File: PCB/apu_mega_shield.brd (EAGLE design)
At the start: 108 x 54.4 mm, 46 parts, among them IC1 74AHC573, IC2 4050D, IC3 DS1307, IC4 LP298XS, Q1 32.768, U1 IS62C1024AL, X1 MICROSDMOLEX

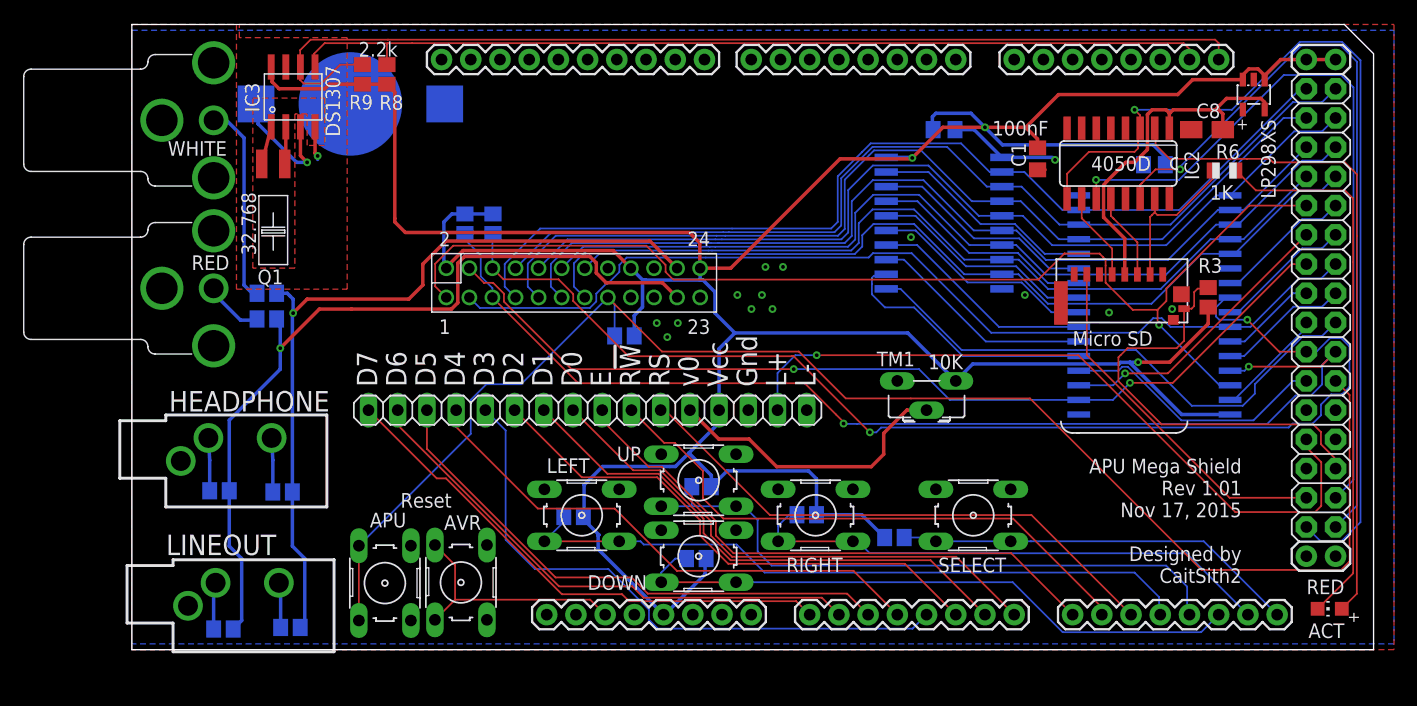
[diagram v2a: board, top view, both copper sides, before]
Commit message: Tweaked reset button layouts.  On the module version of the board, SD card connector and its supporting components moved.
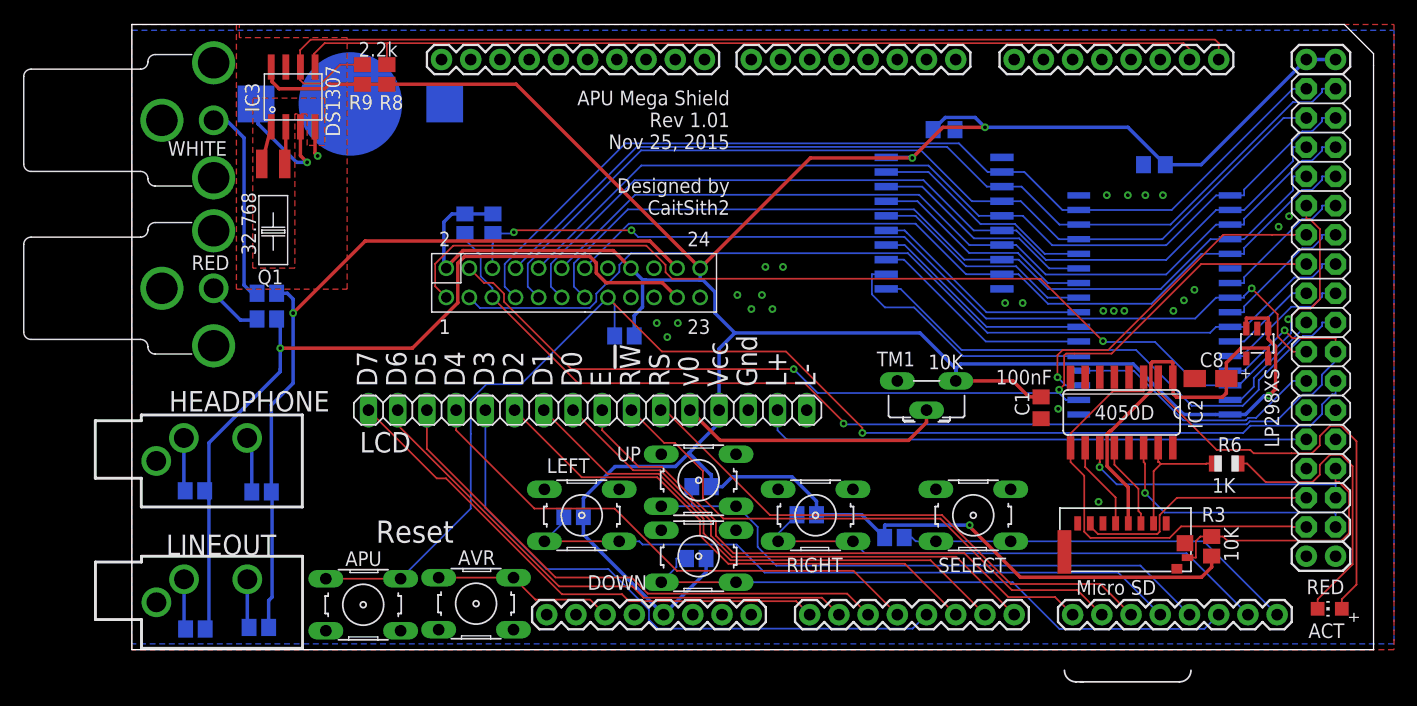
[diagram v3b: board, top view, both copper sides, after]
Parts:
- moved R6 25.5 mm to (95.2, 16.2)
- moved C8 21.6 mm to (93.8, 23.6)
- moved C1 21.6 mm to (79.0, 21.0)
- moved IC2 21.6 mm to (86.1, 20.6)
- moved IC4 21.6 mm to (97.8, 26.6)
- moved R3 21.6 mm to (93.9, 8.99)
- moved X1 21.6 mm to (81.1, 6.81)
- moved U$3 2.76 mm to (6.84, 4.12)
- moved C5 2.74 mm to (11.0, 1.94)
- moved APU 2.66 mm to (20.1, 3.91), turned to 180 degrees
- moved C6 2.44 mm to (5.52, 1.80)
- moved AVR 2.27 mm to (29.9, 4.00), turned to 180 degrees
- moved R5 2.13 mm to (5.49, 13.8)
- moved U$2 2.13 mm to (6.82, 16.4)
- moved R4 1.83 mm to (11.3, 13.7)
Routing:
- net CS: track 67.0 -> 22.5 mm
- net CLK: track 81.7 -> 38.1 mm, vias 1 -> 0
- net DI: track 64.6 -> 24.0 mm
- net !RD: track 105.5 -> 81.6 mm, vias 2 -> 3
- net N$11: track 48.1 -> 26.2 mm
- net BUF_LED: track 58.4 -> 37.8 mm
- net RST: track 133.2 -> 115.2 mm, vias 0 -> 1
- net VCC: track 314.0 -> 331.1 mm, vias 3 -> 4
- net CD: track 37.9 -> 22.3 mm
- net N$14: track 63.3 -> 48.1 mm, vias 1 -> 0
- net GND: track 13.4 -> 2.63 mm, vias 15 -> 26
- net DO: track 31.2 -> 21.5 mm
- net N$1: track 21.5 -> 15.8 mm
- net A13: track 25.2 -> 30.1 mm
- net A11: track 82.8 -> 85.9 mm
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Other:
- board text added: "APU Mega Shield Rev 1.01 Nov 25, 2015 Designed by CaitSith2"
- board text removed: "APU Mega Shield Rev 1.01 Nov 17, 2015 Designed by CaitSith2"

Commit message: Final revisions to the PCB design, hopefully. :)
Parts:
- added C9: 100nF, apu_pcb:C0805
- C1, C2, C7: device rcl:C0805 -> apu_pcb:C0805
- C3, C4, C5, C6: device resistor:C0805 -> apu_pcb:C0805
- R10, R11, R12, R13, R14, R15, R2, R3, R4, R5, R7, R8, R9: device resistor:R0805 -> adafruit:R0805
- moved U1 2.41 mm to (88.9, 32.4)
- moved C2 1.91 mm to (88.9, 44.1)
- moved R3 0.35 mm to (94.2, 8.84)
- moved IC1 0.25 mm to (70.6, 36.8)
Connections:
- net A11: now also U1.3; no longer U1.2
- net A13: now also U1.4; no longer U1.3
- net A17: now also U1.2; no longer U1.4
- net GND: now also C9.1
- net VCC: now also C9.2
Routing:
- net !WR: track 101.0 -> 86.1 mm
- net N$15: track 10.8 -> 18.6 mm
- net VCC: track 331.1 -> 337.9 mm, vias 4 -> 5
- net A13: track 30.1 -> 23.7 mm
- net A15: track 99.3 -> 93.0 mm
- net A7: track 23.2 -> 18.6 mm
- net RST: track 115.2 -> 111.5 mm
- net !RD: track 81.6 -> 85.1 mm, vias 3 -> 2
- net D4: track 79.6 -> 76.9 mm
- net D6: track 76.6 -> 73.8 mm
- net D7: track 74.8 -> 72.3 mm
- net D3: track 80.9 -> 78.4 mm
- net D5: track 77.8 -> 75.3 mm
- net D1: track 83.5 -> 81.4 mm
- net A11: track 85.9 -> 83.9 mm, vias 2 -> 1
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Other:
- outline, holes or cut-outs redrawn
- board text added: "APU Mega Shield Rev 1.02 Dec 15, 2015 Designed by CaitSith2"
- board text removed: "APU Mega Shield Rev 1.01 Nov 25, 2015 Designed by CaitSith2"
